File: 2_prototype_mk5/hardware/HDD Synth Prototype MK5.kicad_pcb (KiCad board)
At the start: 2 copper layers, 100.3 x 69.9 mm, 47 parts, among them J1 Micro_SD_Card, J2 SATA00102253A, J6 171825-4, J7 Conn_01x04_Pin, J8 Conn_01x05, Q1 2N7002, U1 MAX98357A, U2 Optocoupler_DC_PhotoNPN_AKEC

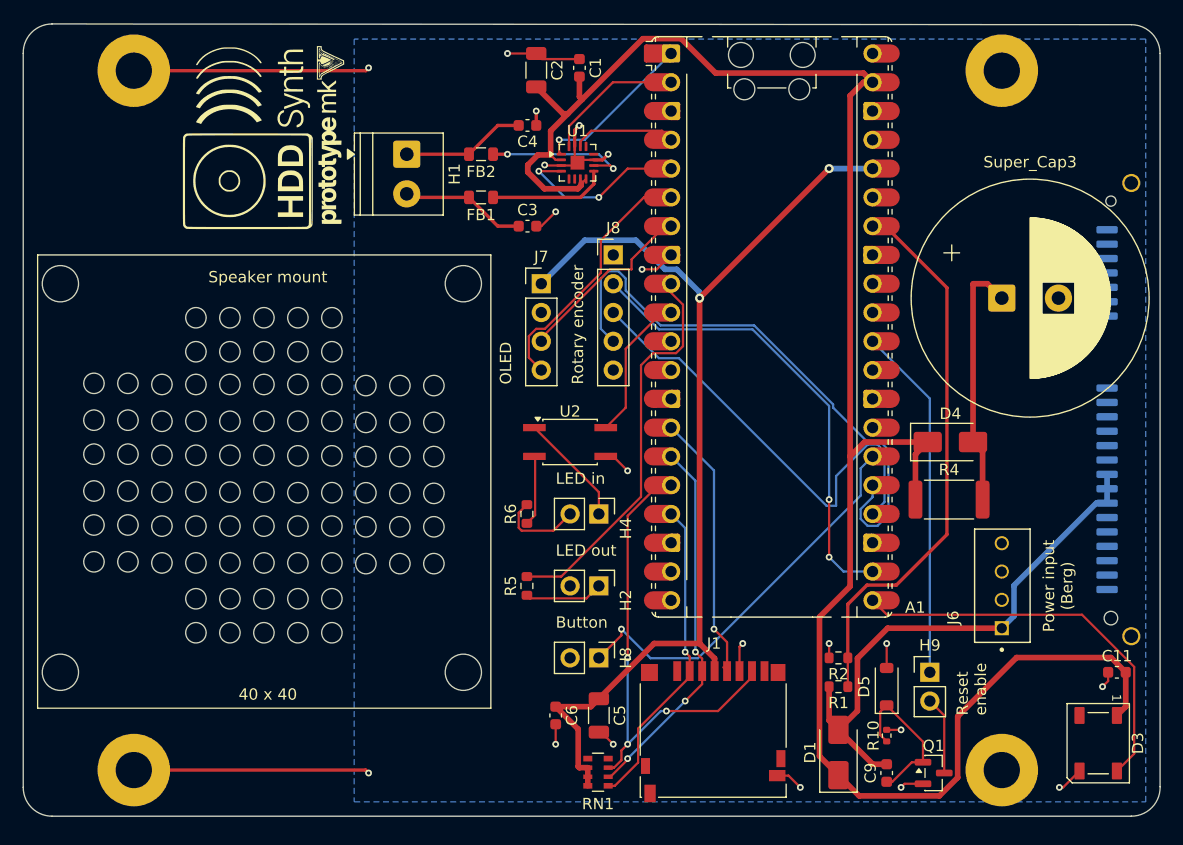
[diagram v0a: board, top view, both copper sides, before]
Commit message: Major MKV redesign using embedded RP2350
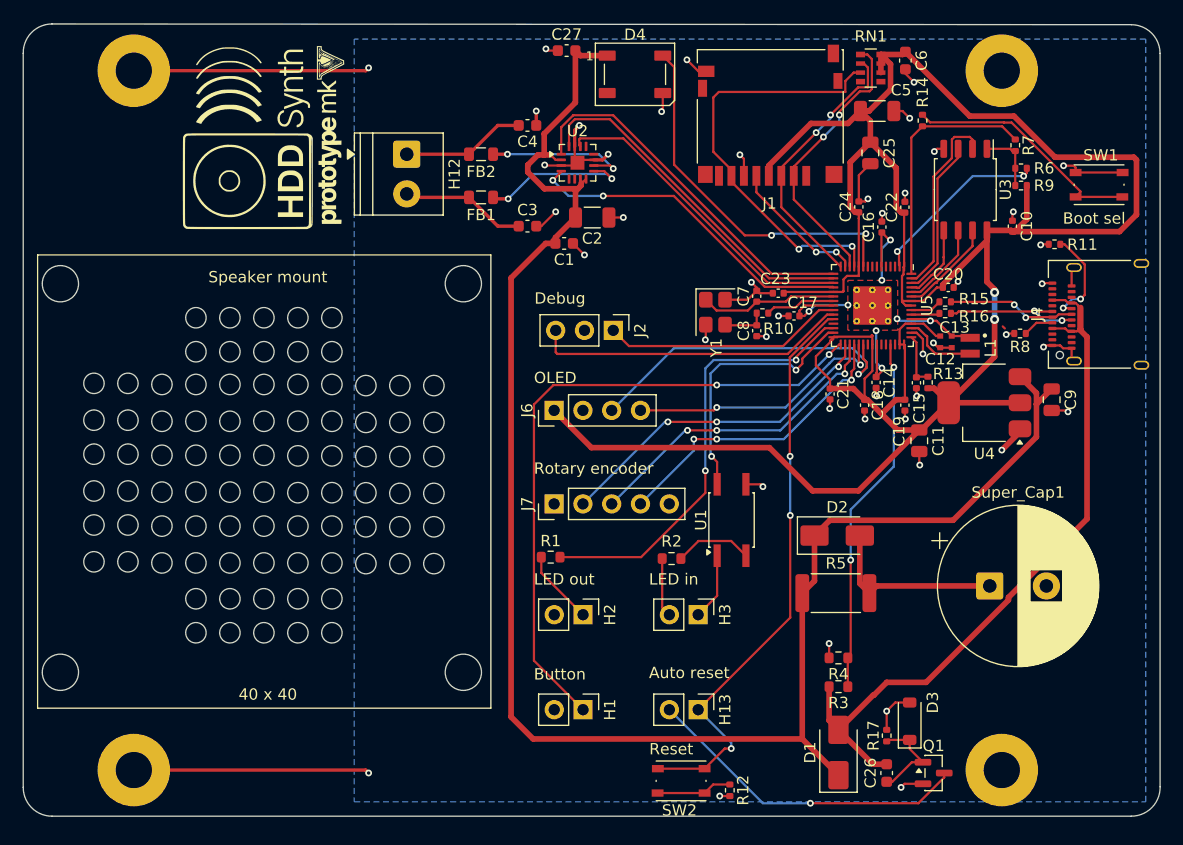
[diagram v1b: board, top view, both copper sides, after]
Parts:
- removed A1: RaspberryPi_Pico2, Module:RaspberryPi_Pico_Common_Unspecified
- removed D5: 1N4148W, Diode_SMD:D_SOD-123
- removed the J6 at (160.0, 100.2)
- removed J8: Conn_01x05, Connector_PinHeader_2.54mm:PinHeader_1x05_P2.54mm_Vertical
- removed Super_Cap3: 1F, Capacitor_THT:CP_Radial_D14.0mm_P5.00mm
- added C10: 100n, Capacitor_SMD:C_0402_1005Metric, F.Cu at (161.0, 64.8)
- added C11: 10u, Capacitor_SMD:C_0805_2012Metric, F.Cu at (152.7, 83.7)
- added C12: 4.7u, RP2350:C_0402_1005Metric_small_pads, F.Cu at (154.6, 75.0)
- added C13: 4.7u, RP2350:C_0402_1005Metric_small_pads, F.Cu at (155.6, 75.0)
- added C14: 100n, Capacitor_SMD:C_0402_1005Metric, F.Cu at (148.9, 78.6)
- added C15: 4.7u, Capacitor_SMD:C_0402_1005Metric, F.Cu at (152.5, 78.6)
- added C16: 4.7u, Capacitor_SMD:C_0402_1005Metric, F.Cu at (149.4, 64.8)
- added C17: 100n, Capacitor_SMD:C_0402_1005Metric, F.Cu at (141.7, 72.7)
- added C18: 100n, Capacitor_SMD:C_0402_1005Metric, F.Cu at (147.9, 80.6)
- added C19: 100n, Capacitor_SMD:C_0402_1005Metric, F.Cu at (151.5, 80.6)
- added C20: 100n, Capacitor_SMD:C_0402_1005Metric, F.Cu at (155.3, 70.2)
- added C21: 100n, Capacitor_SMD:C_0402_1005Metric, F.Cu at (144.9, 79.6)
- added C22: 100n, Capacitor_SMD:C_0402_1005Metric, F.Cu at (151.5, 63.1)
- added C23: 100n, Capacitor_SMD:C_0402_1005Metric, F.Cu at (140.3, 70.7)
- added C24: 100n, Capacitor_SMD:C_0402_1005Metric, F.Cu at (147.4, 63.1)
- added C25: 10u, Capacitor_SMD:C_0805_2012Metric, F.Cu at (148.4, 58.3)
- added C7: 15p, Capacitor_SMD:C_0402_1005Metric, F.Cu at (138.4, 71.0)
- added C8: 15p, Capacitor_SMD:C_0402_1005Metric, F.Cu at (138.4, 74.0)
- added C9: 10u, Capacitor_SMD:C_0805_2012Metric, F.Cu at (164.4, 80.1)
- added D3: 1N4148W, Diode_SMD:D_SOD-123, F.Cu at (151.9, 108.5)
- added J4: USB_C_Receptacle_USB2.0_16P, Connector_USB:USB_C_Receptacle_Amphenol_12401610E4-2A, F.Cu at (169.5, 72.5)
- added J7: Conn_01x05, Connector_PinHeader_2.54mm:PinHeader_1x05_P2.54mm_Vertical, F.Cu at (120.5, 89.3)
- added L1: 3.3u, RP2350:L_pol_2016, F.Cu at (157.2, 75.3)
- added R10: 1k, Resistor_SMD:R_0402_1005Metric, F.Cu at (138.9, 72.4)
- added R11: 5.1K, Resistor_SMD:R_0402_1005Metric, F.Cu at (164.7, 66.4)
- added R12: 1k, Resistor_SMD:R_0402_1005Metric, F.Cu at (136.0, 114.6)
- added R13: 33, Resistor_SMD:R_0402_1005Metric, F.Cu at (153.5, 78.6)
- added R14: 1k, Resistor_SMD:R_0402_1005Metric, F.Cu at (153.0, 55.4)
- added R15: 27, Resistor_SMD:R_0402_1005Metric, F.Cu at (155.0, 71.5)
- added R16: 27, Resistor_SMD:R_0402_1005Metric, F.Cu at (155.0, 72.5)
- added R6: DNF, Resistor_SMD:R_0402_1005Metric, F.Cu at (161.7, 59.7)
- added R7: 0, Resistor_SMD:R_0402_1005Metric, F.Cu at (161.2, 57.6)
- added R8: 5.1K, Resistor_SMD:R_0402_1005Metric, F.Cu at (161.6, 74.2)
- added R9: DNF, Resistor_SMD:R_0402_1005Metric, F.Cu at (161.7, 61.2)
- added SW1: SW_Push, Button_Switch_SMD:SW_Push_1P1T_NO_Vertical_Wuerth_434133025816, F.Cu at (168.6, 61.1)
- added SW2: SW_Push, Button_Switch_SMD:SW_Push_1P1T_NO_Vertical_Wuerth_434133025816, F.Cu at (131.7, 113.7)
- added Super_Cap1: 1F, Capacitor_THT:CP_Radial_D14.0mm_P5.00mm, F.Cu at (159.0, 96.5)
- added U3: W25Q128JVS, RP2350:SOIC-8_5.23x5.23mm_P1.27mm, F.Cu at (156.8, 61.5)
- added U4: NCP1117-3.3_SOT223, Package_TO_SOT_SMD:SOT-223-3_TabPin2, F.Cu at (158.5, 80.4)
- added U5: RP2350_60QFN, RP2350:RP2350-QFN-60-1EP_7x7_P0.4mm_EP3.4x3.4mm_ThermalVias, F.Cu at (148.6, 71.8)
- added Y1: ABM8-272-T3, Crystal:Crystal_SMD_3225-4Pin_3.2x2.5mm, F.Cu at (134.7, 72.4)
- J2: value SATA00102253A -> Conn_01x03; footprint Connector_SATA_SAS:SATA_Amphenol_10029364-001LF_Horizontal -> Connector_PinHeader_2.54mm:PinHeader_1x03_P2.54mm_Vertical; moved to F.Cu
- moved C27 73.3 mm to (121.6, 49.3)
- moved D4 71.8 mm to (127.6, 51.4), turned to 0 degrees
- moved RN1 66.6 mm to (148.5, 50.8), turned to 0 degrees
- moved C6 65.5 mm to (151.5, 50.2)
- moved C5 58.7 mm to (149.0, 54.6), turned to 0 degrees
- moved J1 54.6 mm to (139.6, 55.0), turned to 0 degrees
- moved J2 45.1 mm to (125.7, 74.0), turned to -90 degrees
- moved G*** 24.0 mm to (143.3, 102.0)
- moved H13 20.7 mm to (133.2, 107.4), turned to -90 degrees
- moved U1 15.8 mm to (136.2, 90.7), turned to 90 degrees
- moved C1 15.6 mm to (121.4, 66.3), turned to 180 degrees
- moved C2 13.9 mm to (123.9, 64.0), turned to 180 degrees
- moved R2 13.4 mm to (130.9, 94.1), turned to 180 degrees
- moved R5 13.0 mm to (145.4, 97.2)
- moved D2 13.0 mm to (145.5, 92.1)
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- renumbered C9 to C26, C11 to C27, D4 to D2, D3 to D4, H8 to H1, H6 to H10, H7 to H11, H1 to H12, H9 to H13, H4 to H3, H10 to H4, H11 to H5, H12 to H6, H13 to H7, H3 to H8, H5 to H9, J7 to J6, R5 to R1, R10 to R17, R6 to R2, R1 to R3, R2 to R4, R4 to R5, U2 to U1, U1 to U2
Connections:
- net +3.3V renamed +3V3
- net /SD card reader/SD_CS renamed /RP2350/SD_CS
- net /SD card reader/SD_MISO renamed /RP2350/SD_MISO
- net /SD card reader/SD_MOSI renamed /RP2350/SD_MOSI
- net /VCC_DETECT renamed /Power/VCC_DETECT
- D4 pad 4: /RGB LED/RGB_DATA -> /RP2350/LED_DATA
- H13 pad 1: /Reset/PICO_RUN -> /RP2350/RUN
- J1 pad 5: /SD card reader/SD_CLK -> /RP2350/SD_SCK
- J6 pad 3: /OLED/OLED_SCL -> /RP2350/OLED_SCL
- J6 pad 4: /OLED/OLED_SDA -> /RP2350/OLED_SDA
- U2 pad 1: /Amplifer/DIN -> /RP2350/AMP_DIN
- U2 pad 14: /Amplifer/LRCLK -> /RP2350/AMP_LRCL
- U2 pad 16: /Amplifer/BCLK -> /RP2350/AMP_BCLK
- U2 pad 4: /Amplifer/SD_MODE -> /RP2350/AMP_SDMODE
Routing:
- net +3V3: track 95.8 -> 226.1 mm
- net /RP2350/RUN: track 0.00 -> 51.6 mm, vias 0 -> 3
- net /Rotary encoder/ENC_SWITCH: track 51.2 -> 0.00 mm
- net /Rotary encoder/ENC_A: track 41.2 -> 0.00 mm, vias 2 -> 0
- net /Rotary encoder/ENC_B: track 41.0 -> 0.00 mm
- net GND: track 86.0 -> 121.7 mm, vias 20 -> 45
- net /RGB LED/RGB_DATA: track 35.3 -> 0.00 mm
- net /RP2350/AMP_DIN: track 0.00 -> 32.6 mm
- net /RP2350/LED_DATA: track 0.00 -> 32.6 mm, vias 0 -> 2
- net +1V1: track 0.00 -> 32.6 mm, vias 0 -> 8
- net /Reset/PICO_RUN: track 31.3 -> 0.00 mm
- net /RP2350/AMP_BCLK: track 0.00 -> 31.2 mm
- net /RP2350/OLED_SCL: track 0.00 -> 29.8 mm, vias 0 -> 1
- net /RP2350/AMP_SDMODE: track 0.00 -> 29.8 mm, vias 0 -> 2
- net /RP2350/ENC_A: track 0.00 -> 29.8 mm, vias 0 -> 3
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- added copper zone on F.Cu, net +1V1
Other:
- rule pad_to_mask_clearance: 0 -> 0.051
- board text added: "Auto reset"
- board text added: "Boot sel"
- board text added: "Debug"
- board text added: "Reset"
- board text removed: "Power input (Berg)"
- board text removed: "Power input (SATA)"
- board text removed: "Reset enable"

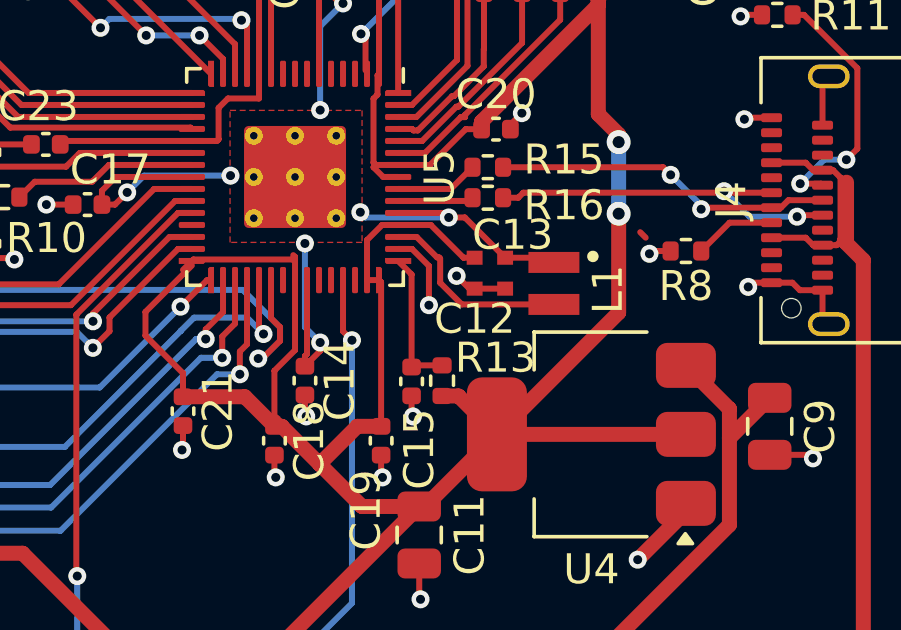
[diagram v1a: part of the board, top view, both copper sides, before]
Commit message: MKV: Add LCSC numbers and resolve DRC errors
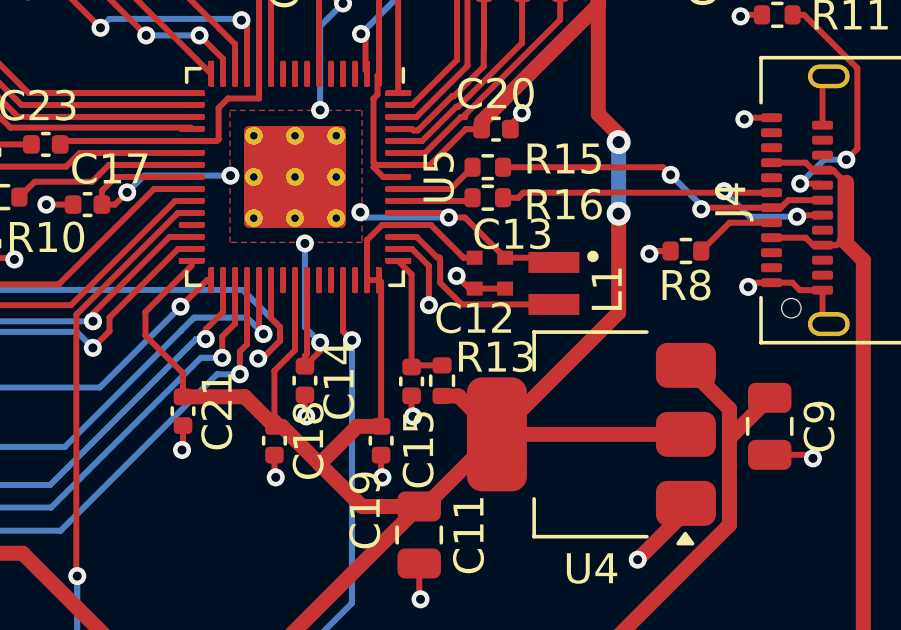
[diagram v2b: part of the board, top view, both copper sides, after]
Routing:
- net +3V3: track 226.1 -> 221.3 mm
- net POWER_5V_SUP: track 156.8 -> 155.3 mm
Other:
- board text added: "Nostalgia by Peter Bridger www.strifestreams.com/hddsynth"
- board text removed: "Peter Bridger www.strifestreams.com/hddsynth"
